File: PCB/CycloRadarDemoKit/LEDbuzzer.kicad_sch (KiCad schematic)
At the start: 19 parts, among them Q301 L8050QLT1G

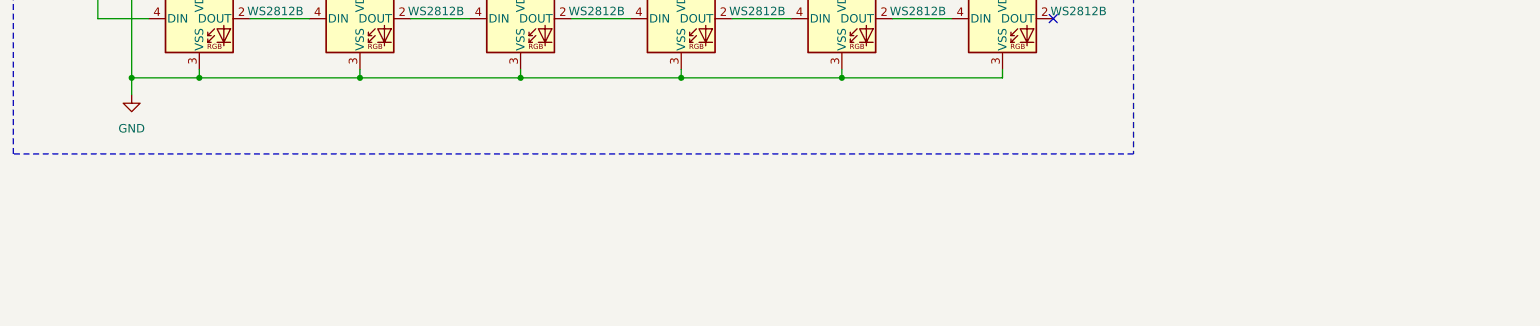
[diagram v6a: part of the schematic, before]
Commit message: Sematic Versioning implemented, whish list added
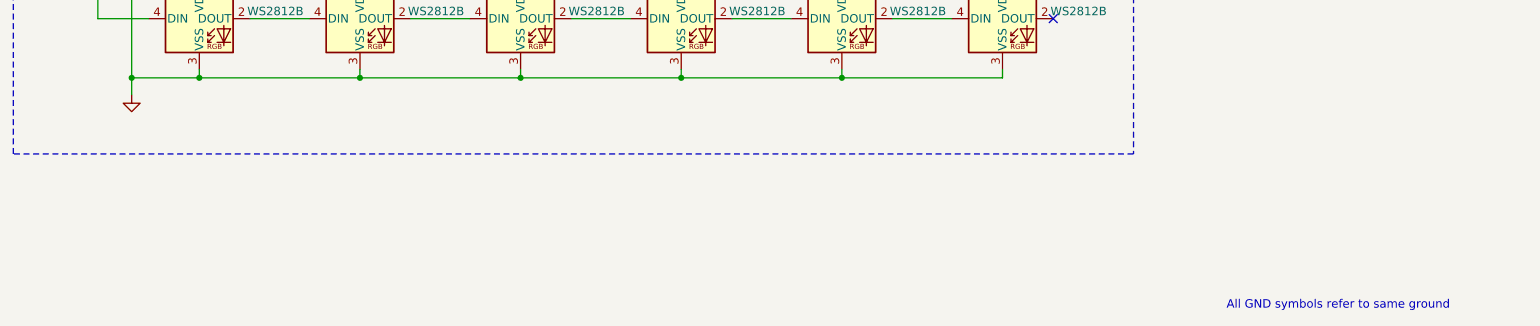
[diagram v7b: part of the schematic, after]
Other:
- note added: "All GND symbols refer to same ground"
- company: ALPS Electric Czech, s.r.o. -> ${COMPANY}
- title: Radar Safety Sensor -> ${TITLE}
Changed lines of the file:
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@@
   (paper "A4")
   (title_block
-    (title "Radar Safety Sensor")
-    (date "2023-12-20")
-    (rev "Rev.: 1.0")
-    (company "ALPS Electric Czech, s.r.o.")
-    (comment 1 "Designed by Martin Tavoda")
+    (title "${TITLE}")
+    (date "${DATE}")
+    (rev "${REVISION}")
+    (company "${COMPANY}")
+    (comment 1 "${CREATOR}")
+    (comment 2 "${APPROVER}")
+    (comment 3 "${STATUS}")
+    (comment 4 "${LANG}")
+    (comment 5 "${NOTE}")
   )
   (junction (at 80.645 99.06) (diameter 0) (color 0 0 0 0)
@@
   (text "RGB LEDs" (at 65.405 88.9 0)
     (effects (font (size 2 2) (thickness 0.4) bold) (justify left bottom))
+  )
+  (text "All GND symbols refer to same ground" (at 243.84 178.435 0)
+    (effects (font (size 1.27 1.27)) (justify left bottom))
   )
   (text "Photoresistor" (at 93.98 26.67 0)
@@
     )
     (property "Value" "GND" (at 79.375 151.13 0)
-      (effects (font (size 1.27 1.27)))
+      (effects (font (size 1.27 1.27)) hide)
     )
     (property "Footprint" "" (at 79.375 146.05 0)

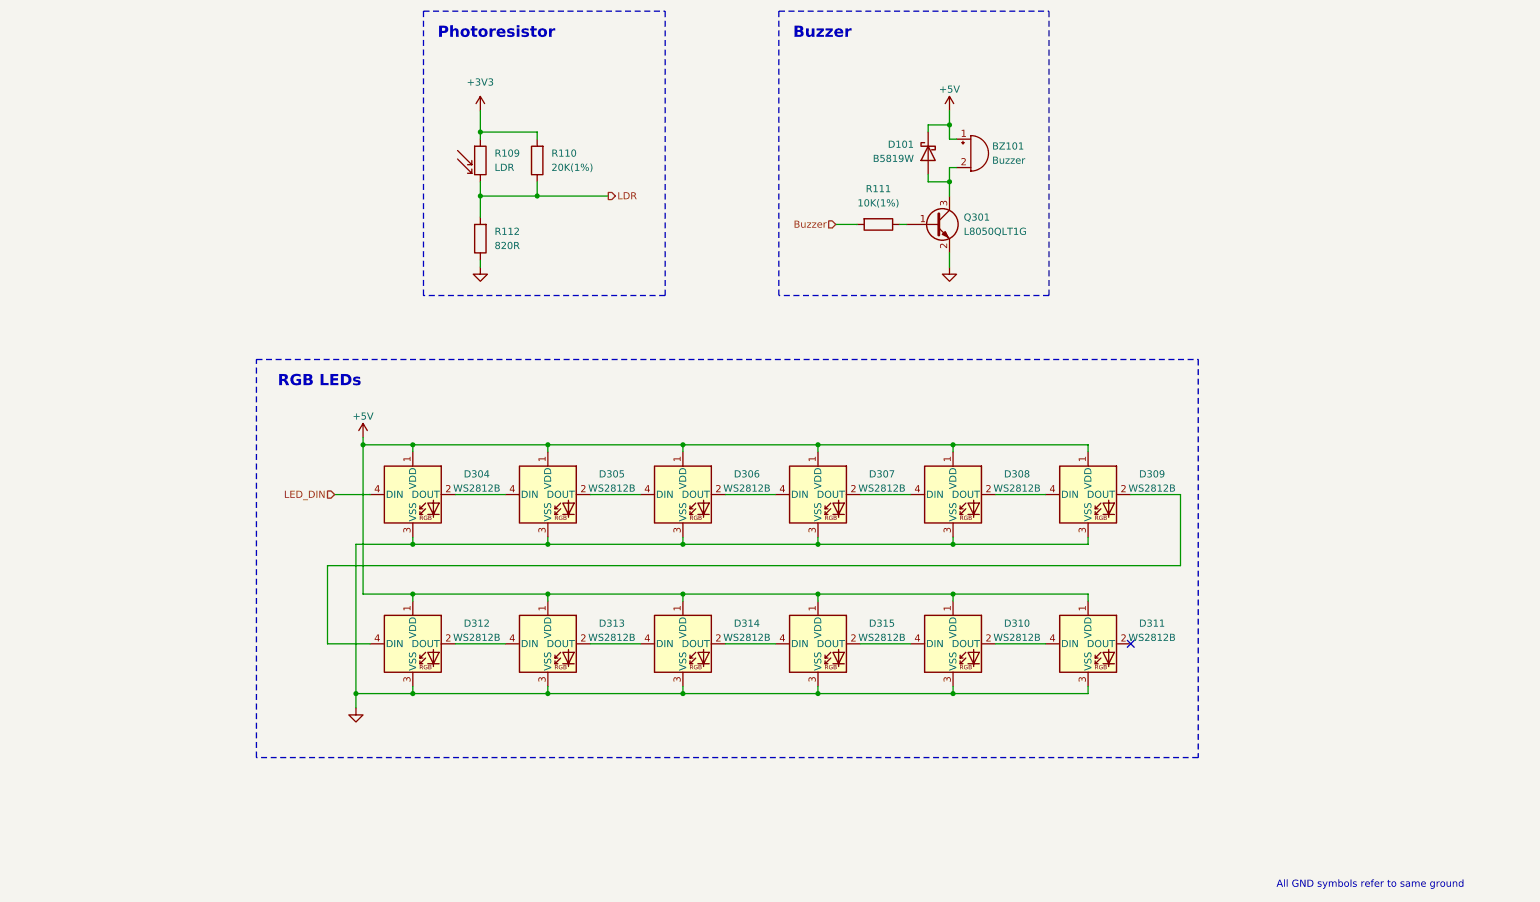
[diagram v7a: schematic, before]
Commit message: photos added, readme rewrited
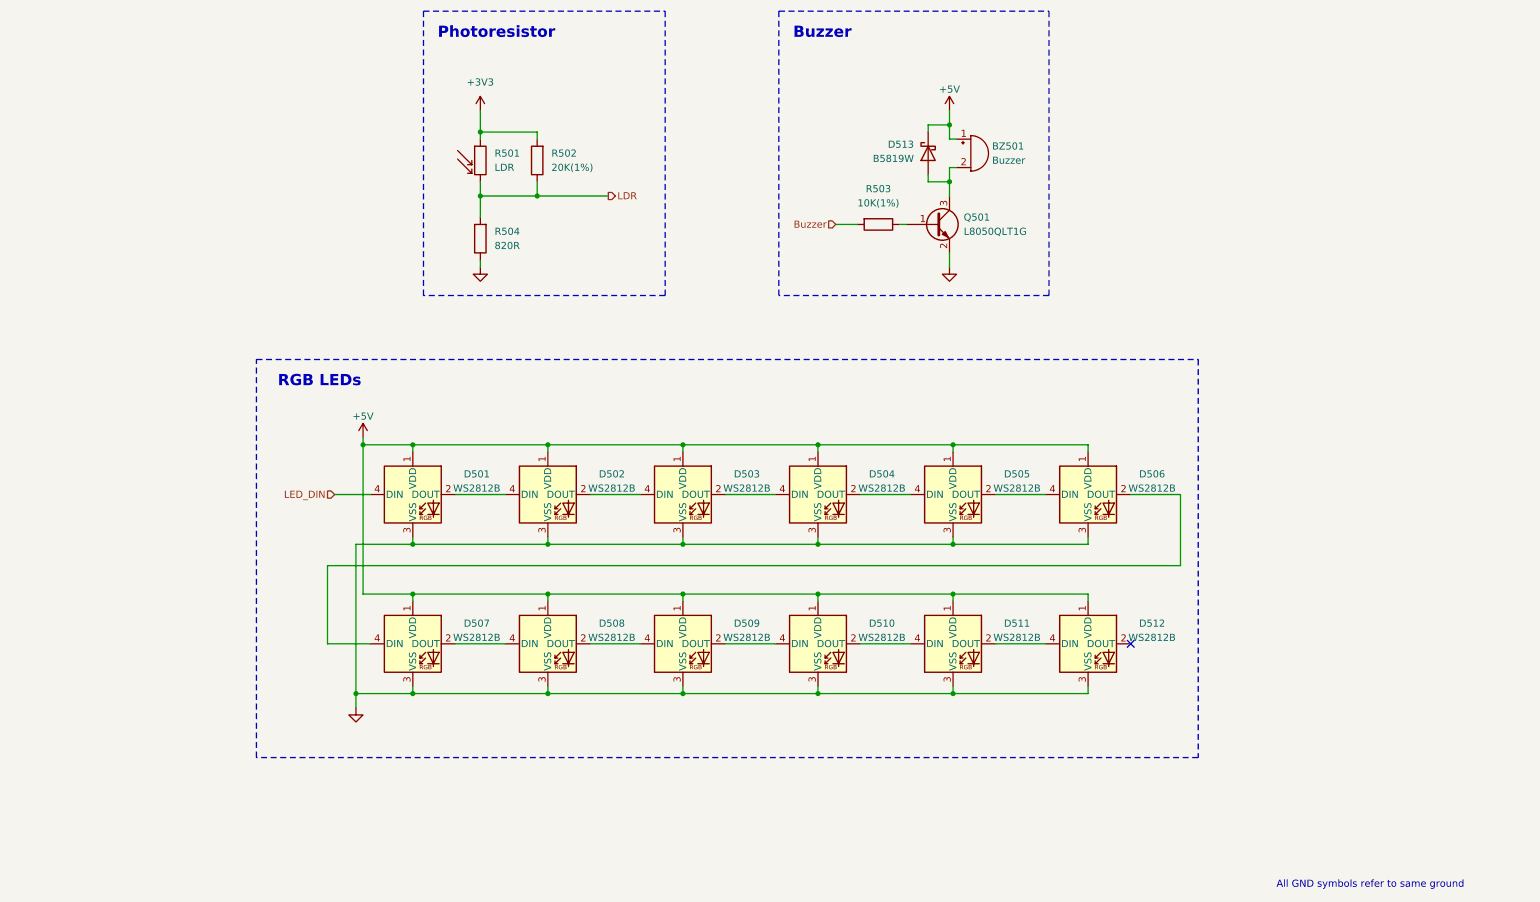
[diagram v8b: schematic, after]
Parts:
- renumbered BZ101 to BZ501, D304 to D501, D305 to D502, D306 to D503, D307 to D504, D308 to D505, D309 to D506, D312 to D507, D313 to D508, D314 to D509, D315 to D510, D310 to D511, D311 to D512, D101 to D513, Q301 to Q501, R109 to R501, R110 to R502, R111 to R503, R112 to R504
